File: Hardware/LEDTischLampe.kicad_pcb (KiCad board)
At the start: 2 copper layers, 160 x 160 mm, 135 parts, among them J1 Conn_01x02_Socket, J2 USB_C_Receptacle_USB2.0_14P, J3 Conn_02x03_Counter_Clockwise, Q1 P-CHANNEL-MOSFET, SW1 Reset, SW2 User, U1 ESP32-C3-WROOM-02, U2 SY7200AABC, U3 SY7200AABC, U4 SY7200AABC, U5 SY7200AABC, U6 SY7200AABC, U7 RY8310

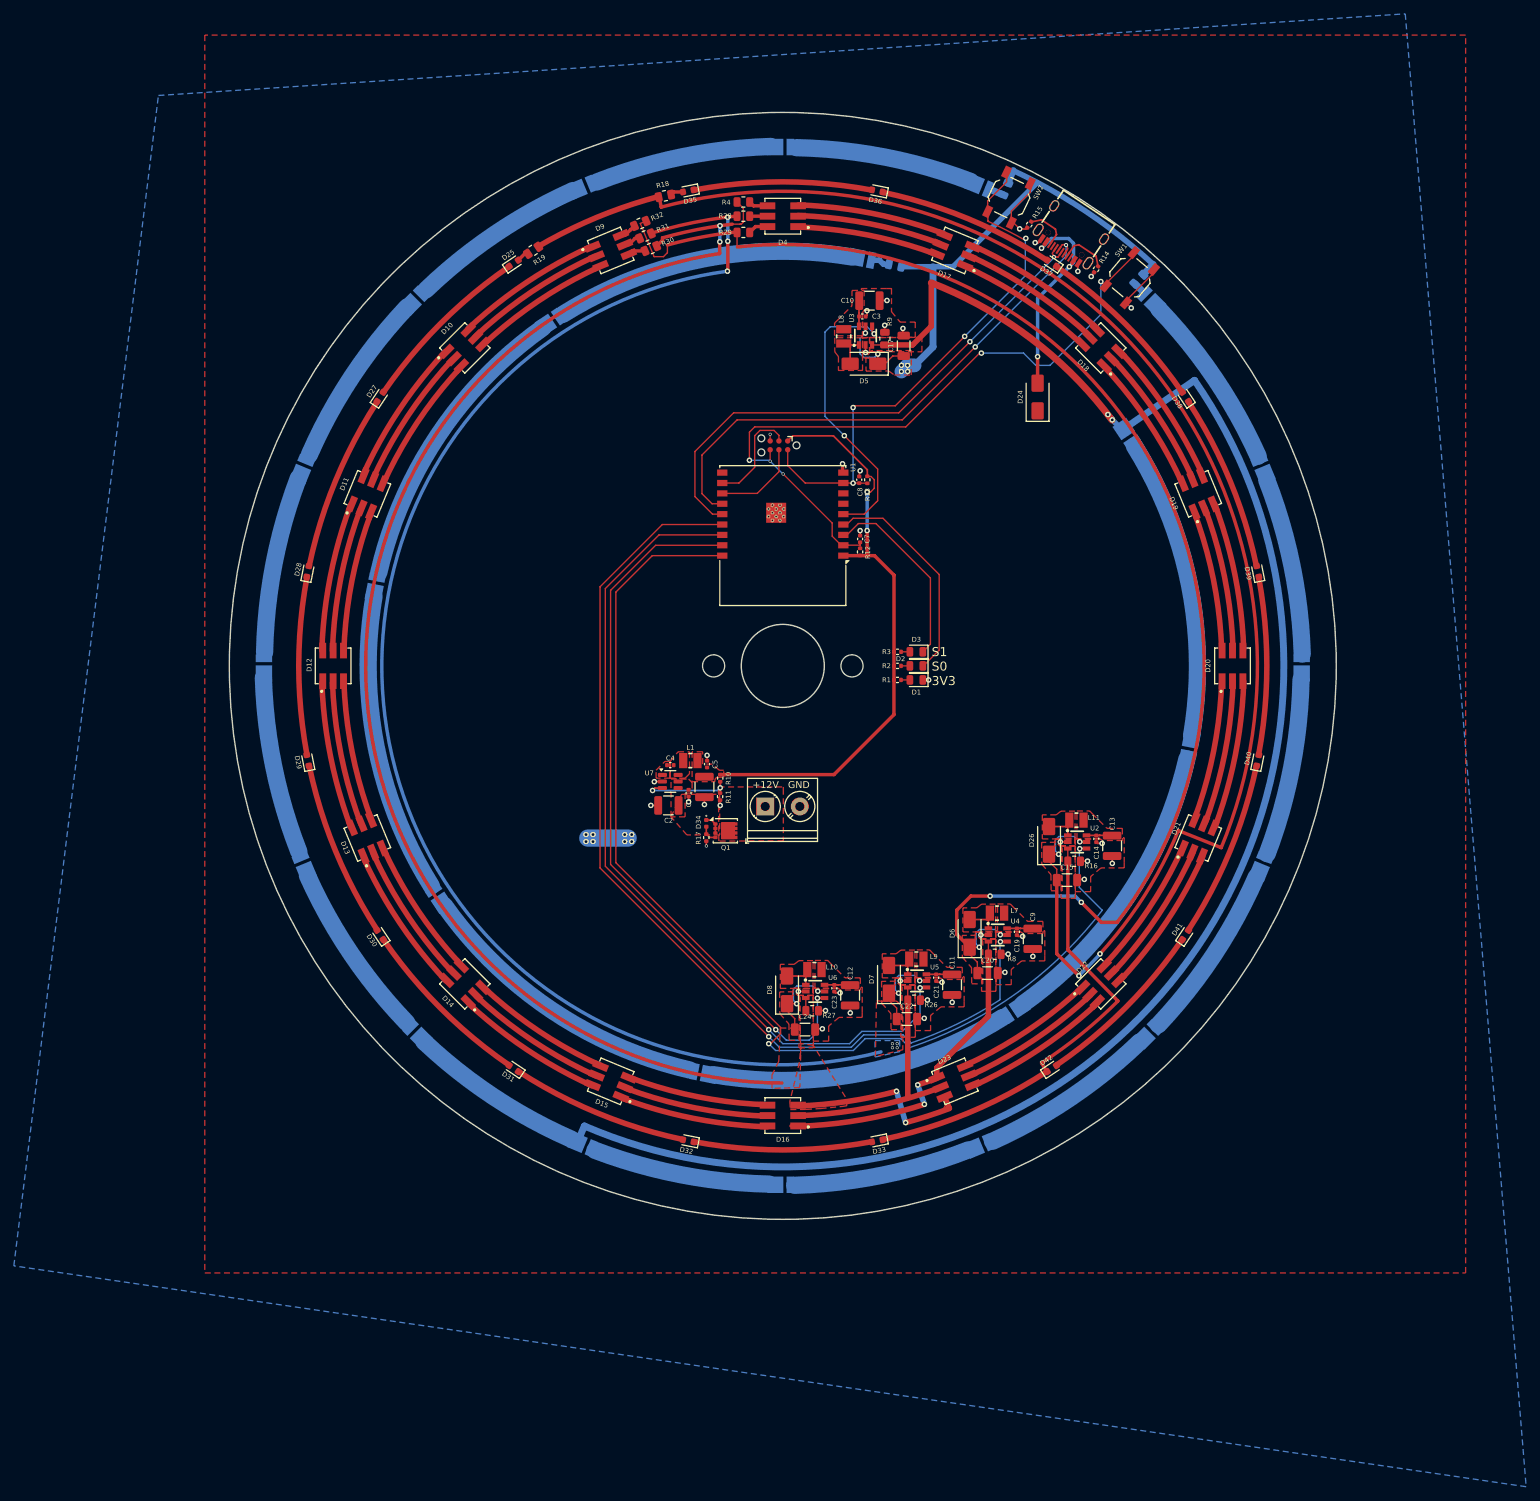
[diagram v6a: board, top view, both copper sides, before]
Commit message: some fixes and BOM optimization, heatsinking, etc
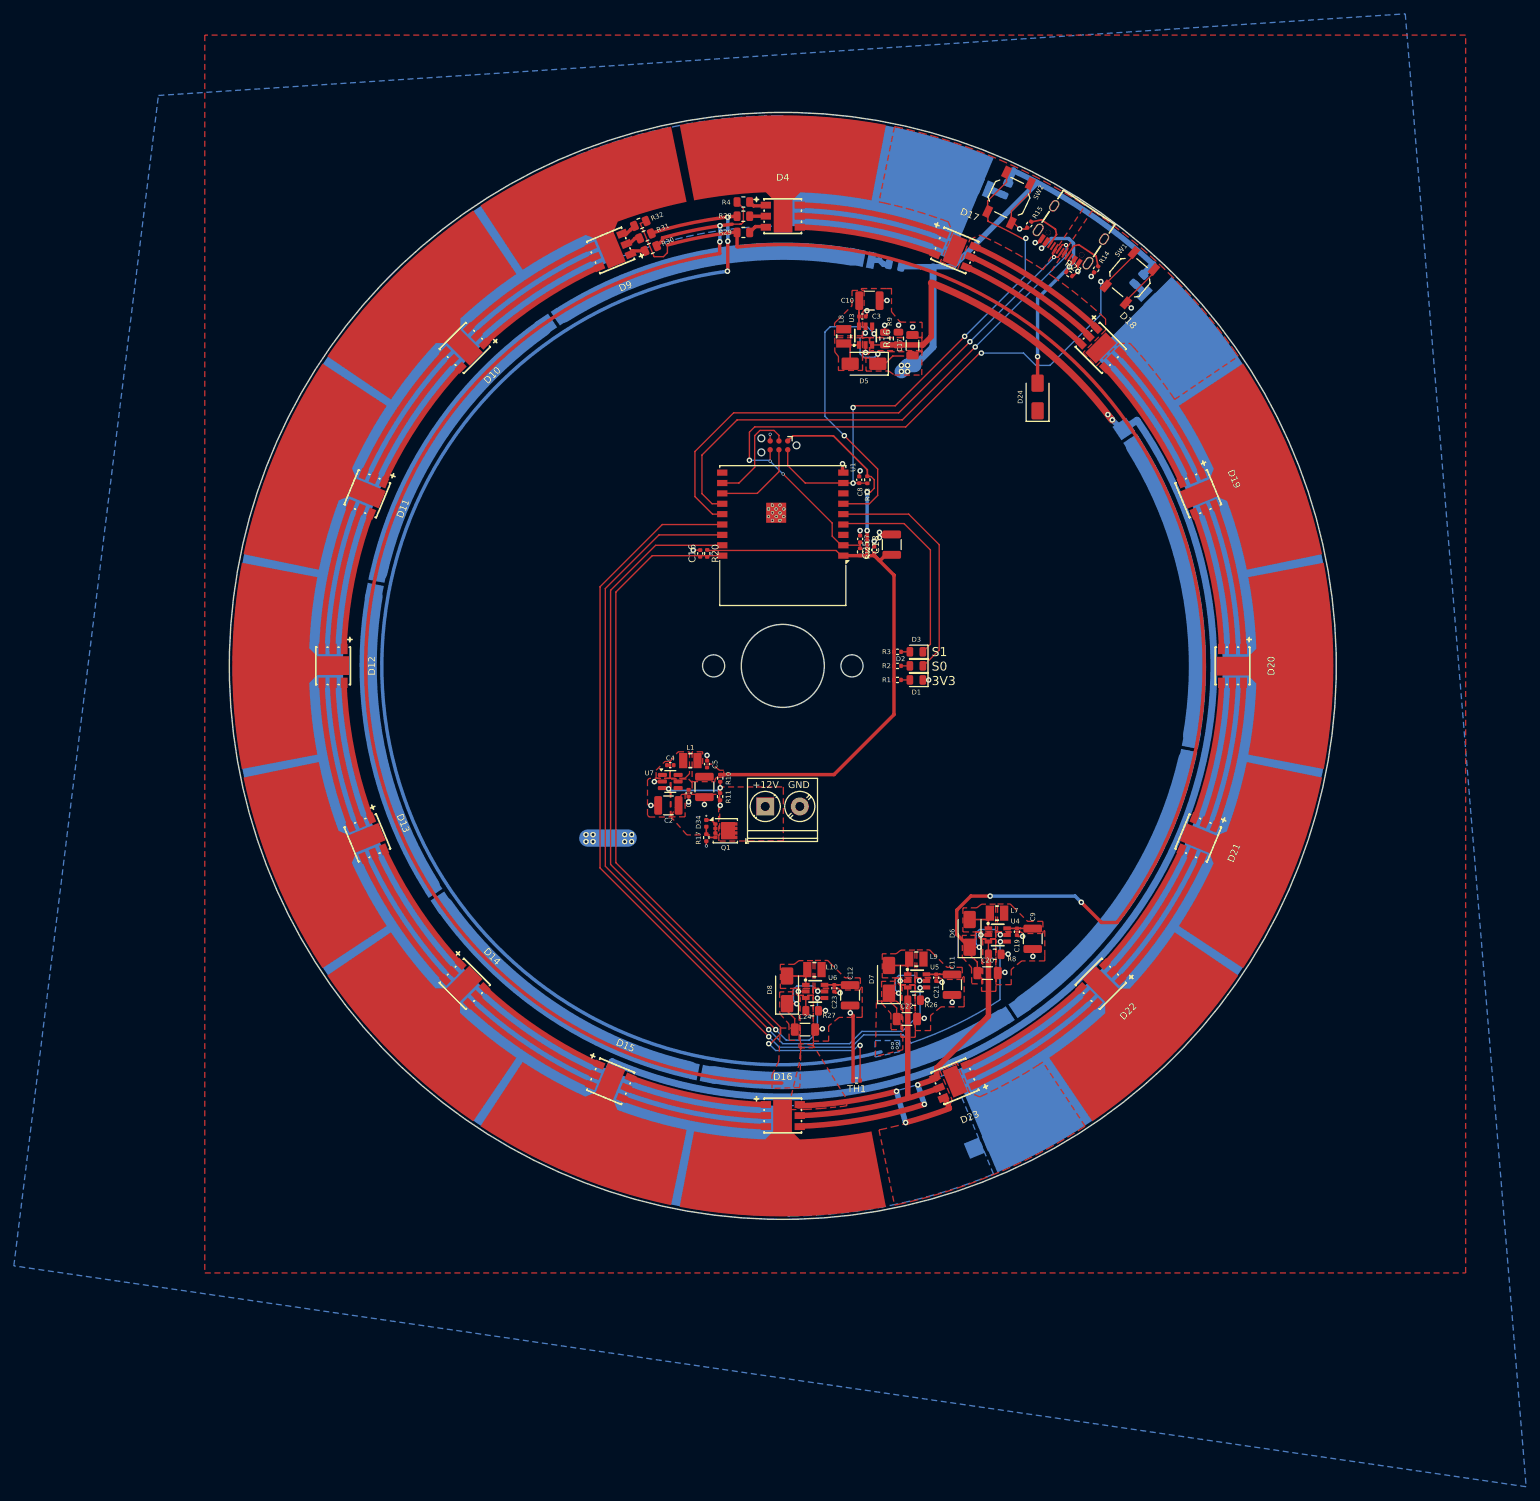
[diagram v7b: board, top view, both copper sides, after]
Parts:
- removed C13: 22u, Capacitor_SMD:C_1210_3225Metric
- removed C14: 100n, Capacitor_SMD:C_0402_1005Metric
- removed C15: 4u7, Capacitor_SMD:C_1206_3216Metric
- removed D25, D27, D28, D29, D30, D31, D32, D33, D35, D36, D37, D38, D39, D40, D41, D42: LED, LED_SMD:LED_0603_1608Metric
- removed D26: SS34, Diode_SMD:D_SMA
- removed L11: 10u, LCSC:IND-SMD_L2.5-W2.0
- removed R18, R19: 22, Resistor_SMD:R_0805_2012Metric
- removed U2: SY7200AABC, LCSC:SOT-23-6_L2.9-W1.6-P0.95-LS2.8-BR
- added C16: 100n, Capacitor_SMD:C_0402_1005Metric, F.Cu at (122.7, 77.7)
- added C18: 22u, Capacitor_SMD:C_1210_3225Metric, F.Cu at (150.4, 76.5)
- added C25: 100n, Capacitor_SMD:C_0402_1005Metric, F.Cu at (147.8, 77.2)
- added R20: 47k, Resistor_SMD:R_0402_1005Metric, F.Cu at (123.7, 77.7)
- added R21: 4k7, Resistor_SMD:R_0402_1005Metric, F.Cu at (176.0, 37.3)
- added TH1: 47k, Resistor_SMD:R_0402_1005Metric, F.Cu at (145.3, 153.9)
- D10, D11, D12, D13, D14, D15, D16, D17, D18, D19, D20, D21, D22, D23, D4, D9: footprint LCSC:LED-SMD_6P-L5.0-W5.0-TL_TC5050RGBF08 -> LCSC:LED-SMD_6P-L5.0-W5.0-BL_TC5053RGBE60
- R16, R26, R27, R8: value 3.3 -> 1
- R28, R29, R30, R31, R32, R4: value 22 -> 10
- R9: value 0.5 -> 1
- moved R16 79.7 mm to (151.3, 46.7), turned to 90 degrees
- moved C17 1.27 mm to (153.4, 47.6)
- turned D10 to -135 degrees
- turned D11 to -112.5 degrees
- turned D12 to -90 degrees
- turned D13 to -67.5 degrees
- turned D14 to -45 degrees
- turned D15 to -22.5 degrees
- turned D16 to 0 degrees
- turned D17 to -22.5 degrees
- turned D18 to -45 degrees
- turned D19 to -67.5 degrees
- turned D20 to -90 degrees
- turned D21 to -112.5 degrees
- turned D22 to -135 degrees
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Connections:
- net Net-(D24-A) renamed VBUS
- D10 pad 2: Net-(D10-GK) -> Net-(D10-+-Pad2)
- D10 pad 5: Net-(D10-GA) -> Net-(D10---Pad5)
- D11 pad 1: Net-(D11-RK) -> Net-(D10-RA)
- D11 pad 2: Net-(D11-GK) -> Net-(D10---Pad5)
- D11 pad 3: Net-(D11-BK) -> Net-(D10-BA)
- D11 pad 4: Net-(D10-BK) -> Net-(D11-BA)
- D11 pad 5: Net-(D10-GK) -> Net-(D11---Pad5)
- D11 pad 6: Net-(D10-RK) -> Net-(D11-RA)
- D12 pad 1: Net-(D12-RK) -> Net-(D11-RA)
- D12 pad 2: Net-(D12-GK) -> Net-(D11---Pad5)
- D12 pad 3: Net-(D12-BK) -> Net-(D11-BA)
- D12 pad 4: Net-(D11-BK) -> Net-(D12-BA)
- D12 pad 5: Net-(D11-GK) -> Net-(D12---Pad5)
- D12 pad 6: Net-(D11-RK) -> Net-(D12-RA)
- D13 pad 1: Net-(D13-RK) -> Net-(D12-RA)
- D13 pad 2: Net-(D13-GK) -> Net-(D12---Pad5)
- D13 pad 3: Net-(D13-BK) -> Net-(D12-BA)
- D13 pad 4: Net-(D12-BK) -> Net-(D13-BA)
- D13 pad 5: Net-(D12-GK) -> Net-(D13---Pad5)
- D13 pad 6: Net-(D12-RK) -> Net-(D13-RA)
- D14 pad 1: Net-(D14-RK) -> Net-(D13-RA)
- D14 pad 2: Net-(D14-GK) -> Net-(D13---Pad5)
- D14 pad 3: Net-(D14-BK) -> Net-(D13-BA)
- D14 pad 4: Net-(D13-BK) -> Net-(D14-BA)
- D14 pad 5: Net-(D13-GK) -> Net-(D14---Pad5)
- D14 pad 6: Net-(D13-RK) -> Net-(D14-RA)
- D15 pad 1: Net-(D15-RK) -> Net-(D14-RA)
- D15 pad 2: Net-(D15-GK) -> Net-(D14---Pad5)
- D15 pad 3: Net-(D15-BK) -> Net-(D14-BA)
- D15 pad 4: Net-(D14-BK) -> Net-(D15-BA)
- D15 pad 5: Net-(D14-GK) -> Net-(D15---Pad5)
- D15 pad 6: Net-(D14-RK) -> Net-(D15-RA)
- D16 pad 1: /LedsOben/LedTreiber1/LEDN -> Net-(D15-RA)
- D16 pad 2: /LedsOben/LedTreiber2/LEDN -> Net-(D15---Pad5)
- D16 pad 3: /LedsOben/LedTreiber3/LEDN -> Net-(D15-BA)
- D16 pad 4: Net-(D15-BK) -> /LedsOben/LedTreiber3/LEDN
- D16 pad 5: Net-(D15-GK) -> /LedsOben/LedTreiber2/LEDN
- D16 pad 6: Net-(D15-RK) -> /LedsOben/LedTreiber1/LEDN
- D17 pad 2: Net-(D17-GK) -> Net-(D17-+-Pad2)
- D17 pad 5: Net-(D17-GA) -> Net-(D17---Pad5)
- D18 pad 1: Net-(D18-RK) -> Net-(D17-RA)
- D18 pad 2: Net-(D18-GK) -> Net-(D17---Pad5)
- D18 pad 3: Net-(D18-BK) -> Net-(D17-BA)
- D18 pad 4: Net-(D17-BK) -> Net-(D18-BA)
- D18 pad 5: Net-(D17-GK) -> Net-(D18---Pad5)
- D18 pad 6: Net-(D17-RK) -> Net-(D18-RA)
- D19 pad 1: Net-(D19-RK) -> Net-(D18-RA)
- D19 pad 2: Net-(D19-GK) -> Net-(D18---Pad5)
- D19 pad 3: Net-(D19-BK) -> Net-(D18-BA)
- D19 pad 4: Net-(D18-BK) -> Net-(D19-BA)
- D19 pad 5: Net-(D18-GK) -> Net-(D19---Pad5)
- D19 pad 6: Net-(D18-RK) -> Net-(D19-RA)
- D20 pad 1: Net-(D20-RK) -> Net-(D19-RA)
- D20 pad 2: Net-(D20-GK) -> Net-(D19---Pad5)
- D20 pad 3: Net-(D20-BK) -> Net-(D19-BA)
- D20 pad 4: Net-(D19-BK) -> Net-(D20-BA)
- D20 pad 5: Net-(D19-GK) -> Net-(D20---Pad5)
- D20 pad 6: Net-(D19-RK) -> Net-(D20-RA)
- D21 pad 1: Net-(D21-RK) -> Net-(D20-RA)
- D21 pad 2: Net-(D21-GK) -> Net-(D20---Pad5)
- D21 pad 3: Net-(D21-BK) -> Net-(D20-BA)
- D21 pad 4: Net-(D20-BK) -> Net-(D21-BA)
- D21 pad 5: Net-(D20-GK) -> Net-(D21---Pad5)
- D21 pad 6: Net-(D20-RK) -> Net-(D21-RA)
- D22 pad 1: Net-(D22-RK) -> Net-(D21-RA)
- D22 pad 2: Net-(D22-GK) -> Net-(D21---Pad5)
- D22 pad 3: Net-(D22-BK) -> Net-(D21-BA)
- D22 pad 4: Net-(D21-BK) -> Net-(D22-BA)
- D22 pad 5: Net-(D21-GK) -> Net-(D22---Pad5)
- D22 pad 6: Net-(D21-RK) -> Net-(D22-RA)
- D23 pad 1: /LedsOben/LedTreiber1/LEDN -> Net-(D22-RA)
- D23 pad 2: /LedsOben/LedTreiber2/LEDN -> Net-(D22---Pad5)
- D23 pad 3: /LedsOben/LedTreiber3/LEDN -> Net-(D22-BA)
- D23 pad 4: Net-(D22-BK) -> /LedsOben/LedTreiber3/LEDN
- D23 pad 5: Net-(D22-GK) -> /LedsOben/LedTreiber2/LEDN
- D23 pad 6: Net-(D22-RK) -> /LedsOben/LedTreiber1/LEDN
- D4 pad 1: Net-(D17-RA) -> Net-(D4-+-Pad1)
- D4 pad 2: Net-(D17-GA) -> Net-(D4-+-Pad2)
- D4 pad 3: Net-(D17-BA) -> Net-(D4-+-Pad3)
- D4 pad 4: Net-(D4-BA) -> Net-(D17-BK)
- D4 pad 5: Net-(D4-GA) -> Net-(D17-+-Pad2)
- D4 pad 6: Net-(D4-RA) -> Net-(D17-RK)
- D9 pad 1: Net-(D10-RA) -> Net-(D9-+-Pad1)
- D9 pad 2: Net-(D10-GA) -> Net-(D9-+-Pad2)
- D9 pad 3: Net-(D10-BA) -> Net-(D9-+-Pad3)
- D9 pad 4: Net-(D9-BA) -> Net-(D10-BK)
- D9 pad 5: Net-(D9-GA) -> Net-(D10-+-Pad2)
- D9 pad 6: Net-(D9-RA) -> Net-(D10-RK)
- R16 pad 1: /LedsOben/LedTreiber5/LEDN -> /LedsUnten/LedTreiber4/LEDN
- R28 pad 2: Net-(D4-GA) -> Net-(D4-+-Pad2)
- R29 pad 2: Net-(D4-RA) -> Net-(D4-+-Pad1)
- R30 pad 2: Net-(D9-BA) -> Net-(D9-+-Pad3)
- R31 pad 2: Net-(D9-GA) -> Net-(D9-+-Pad2)
- R32 pad 2: Net-(D9-RA) -> Net-(D9-+-Pad1)
- R4 pad 2: Net-(D4-BA) -> Net-(D4-+-Pad3)
- U1 pad 18: ADim -> NTC
- U1 pad 3: StateLed01 -> unconnected-(U1-IO4-Pad3)
- U1 pad 4: StateLed00 -> StateLed01
- U1 pad 5: WhiteDim -> StateLed00
- U1 pad 6: unconnected-(U1-IO7-Pad6) -> WhiteDim
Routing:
- net ADim: track 126.8 -> 0.00 mm, vias 2 -> 0
- net NTC: track 0.00 -> 112.6 mm, vias 0 -> 2
- net /LedsOben/LedTreiber5/LEDP: track 28.4 -> 0.00 mm, vias 4 -> 0
- net +3V3: track 85.1 -> 108.6 mm
- net /LedsOben/LedTreiber5/LEDN: track 19.7 -> 0.00 mm
- net GND: track 57.5 -> 69.3 mm
- net Net-(D26-A): track 3.90 -> 0.00 mm
- net VCC: track 27.4 -> 23.6 mm
- net Net-(D4-RA): track 2.93 -> 0.00 mm
- net Net-(D4-+-Pad1): track 0.00 -> 2.93 mm
- net Net-(U7-FB): track 13.2 -> 10.3 mm
- net Net-(D4-BA): track 2.81 -> 0.00 mm
- net Net-(D4-+-Pad3): track 0.00 -> 2.81 mm
- net Net-(D4-GA): track 2.58 -> 0.00 mm
- net Net-(D4-+-Pad2): track 0.00 -> 2.58 mm
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- added copper zone on B.Cu, net Net-(LED14-C)
- added copper zone on B.Cu, net Net-(LED18-C)
- added copper zone on F.Cu, net unconnected-(D18-EP-Pad7)
- added copper zone on F.Cu, net unconnected-(D23-EP-Pad7)
- added copper zone on F.Cu, net unconnected-(D4-EP-Pad7)
- removed copper zone on F.Cu, net /LedsOben/LedTreiber5/LEDN
- removed copper zone on F.Cu, net /LedsOben/LedTreiber5/LEDP
- removed copper zone on F.Cu, net Net-(D26-A)

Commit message: silkscreen and stuff
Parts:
- added ?: , clipboard:7d3e68b6-f38f-4a7e-bad3-74a2474ef35d, F.Cu at (92.1, 92.2)
- added G***: LOGO, LeoDJ-kicad:Logo_PCBDerg_10mm, F.Cu at (93.0, 72.9)
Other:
- board text added: "LeoDJ"
- board text added: "Techbeard"
- board text added: "TheLÄMPAN"
- board text added: "https://github.com/RainbowLabsDE/TheLAEMPAN"
- board text added: "v1.0"
